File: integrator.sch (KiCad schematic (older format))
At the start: 13 parts, among them J1 SJ-3524-SMT, J2 SJ-3524-SMT, SW1 EVQP40B3M, SW2 EVQP40B3M, U1 Teensy3.2, U2 FXOS8700CQ

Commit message: saved before library tweak
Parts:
- removed C1, C2, C3: 0.1uF, Capacitor_SMD:C_0603_1608Metric, symbol Device:CP1_Small
- removed U2: FXOS8700CQ, misc:FSOS8700CQ_PKG, symbol FXOS8700CQ:FXOS8700CQ
- added C1: 10nf, symbol Device:C_Small
- added C2, C5: 0.1uf, symbol Device:C_Small
- added C3: 2.2uf, symbol Device:C_Small
- added C4: 4.7uf, symbol Device:C_Small
- added D1: SD0805S020S1R0, symbol Device:D_Schottky_Small
- added R2, R3, R6: 4.7k, symbol Device:R
- added R4, R5: 5k, symbol Device:R
- added U2: ICM-20600, PQFN50P250X300X97-14N, symbol icm-20600:ICM-20600
- POGO1: value Conn_02x06_Odd_Even_MountingPin -> PO pogos
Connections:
- wire segments 108 -> 136
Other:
- moved on the sheet: J2, LED1, LED2, R1, SW1

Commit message: snapshot everything for safety
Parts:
- added C6: 4.7uf, Capacitor_SMD:CP_Elec_5x4.5, symbol Device:C_Small
- C1, C2, C3, C5: footprint (none) -> Capacitor_SMD:C_0805_2012Metric
- C4: footprint (none) -> Capacitor_SMD:CP_Elec_5x4.5
- D1: footprint (none) -> Diode_SMD:D_0805_2012Metric
- LED1, LED2: footprint LED_SMD:LED_0603_1608Metric -> LED_SMD:LED_0805_2012Metric
- POGO1: footprint Connector_PinSocket_2.54mm:PinSocket_2x06_P2.54mm_Vertical -> Connector_PinSocket_2.54mm:PinSocket_2x06_P2.54mm_Vertical_SMD
- R1: footprint Resistor_SMD:R_0603_1608Metric -> Resistor_SMD:R_0805_2012Metric
- R2, R3, R4, R5, R6: footprint (none) -> Resistor_SMD:R_0805_2012Metric
- U2: symbol icm-20600:ICM-20600 -> ICM-20600:ICM-20600
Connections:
- net Earth: now also SW2.2, C6.2; no longer SW2.1
- net at U1.11 (9_RX2_CS_PWM): now also SW2.1; no longer SW2.2
- net at C1.2, C2.1, C3.1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: now also C4.1, D1.1 (K), U1.31 (3.3V), C6.1; no longer U1.16 (3.3V)
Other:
- moved on the sheet: C1, C2, C3, C4, C5, D1, J1, J2, LED1, LED2, POGO1, R1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

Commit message: snapshot with hackzone
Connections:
- net at U1.2 (0_RX1_Touch): now also SW1.2
- net at U1.5 (3_TX_PWM): no longer SW1.2
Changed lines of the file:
@@
 	6000 2250 1800 2250
-Wire Wire Line
-	6500 3800 6000 3800
-Wire Wire Line
-	6000 3800 6000 2250
 Wire Wire Line
 	2750 1250 5600 1250
@@
 Wire Wire Line
 	8800 6100 8900 6150
-Wire Wire Line
-	6500 3600 5050 3600
-Wire Wire Line
-	5050 3600 5050 3500
-Wire Wire Line
-	5050 3500 1700 3500
 Wire Wire Line
 	1700 3500 1700 4700
@@
 	8600 5900 8800 5900
 Connection ~ 5400 4900
+Wire Wire Line
+	5050 3500 1700 3500
+Wire Wire Line
+	5050 3600 5050 3500
+Wire Wire Line
+	6500 3600 5050 3600
+Wire Wire Line
+	6500 3500 6000 3500
+Wire Wire Line
+	6000 3500 6000 2250
 $EndSCHEMATC

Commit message: last changes of rev3
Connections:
- net r_sync_out: now reaches J2.2, U1.10 (8_TX3_DIN)
- net r_button: now reaches SW2.1, U1.11 (9_RX2_CS_PWM)
- net l_sync_out: now reaches J1.2, U1.13 (11_DOUT)
- net dac: now reaches R4.1, R5.2, U1.19 (A14/DAC)
- net l_button: now reaches SW1.2, U1.2 (0_RX1_Touch)
- net po_play: now reaches POGO1.12 (Pin_12), U1.23 (16_A2_SCL0_Touch)
- net po_wake: now reaches POGO1.6 (Pin_6), U1.24 (17_A3_SDA0_Touch)
- net i2c_sda: now reaches R3.2, U1.25 (18_A4_SDA0_Touch), U2.14 (SDA/SDI)
- net i2c_clk: now reaches R2.2, U1.26 (19_A5_SCL0_Touch), U2.13 (SCL/SCLK)
- net led1: now reaches LED1.2, U1.27 (20_A6_CS_PWM)
- net led2: now reaches LED2.2, U1.28 (21_A7_RX1_CS_PWM)
- net amu_sync: now reaches U1.3 (1_TX1_Touch), U2.10 (FSYNC/NC)
- net +3.3v: now reaches C1.2, C2.1, C3.1, C4.1, C6.1, D1.1 (K), R2.1, R3.1, U1.31 (3.3V), U2.12 (~CS), U2.5 (VDDIO), U2.8 (VDD)
- net a_gnd: now reaches J1.1, J2.1, U1.32 (AGND)
- net amu_int2: now reaches U1.4 (2), U2.9 (INT2)
- net swo: now reaches POGO1.9 (Pin_9), U1.6 (4_RX_PWM)
- net swdio: now reaches POGO1.7 (Pin_7), U1.7 (5_TX1_PWM)
- net swclk: now reaches POGO1.5 (Pin_5), U1.8 (6_PWM)
- net po_reset: now reaches POGO1.3 (Pin_3), R6.2, U1.9 (7_RX3_DOUT)
- net po_batt: now reaches D1.2 (A), POGO1.4 (Pin_4)
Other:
- moved on the sheet: C1, C2, C3, C4, C5, C6, D1, J1, J2, LED1, LED2, POGO1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

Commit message: evt4 schem w/o rocker switches
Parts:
- removed C5: 0.1uf, Capacitor_SMD:C_0805_2012Metric, symbol Device:C_Small
- removed R3: 4.7k, Resistor_SMD:R_0805_2012Metric, symbol Device:R
- added SW3: SW_Push_LED, symbol Switch:SW_Push_LED
- R2: value 4.7k -> 47
- U2: value ICM-20600 -> ICM-42605; footprint PQFN50P250X300X97-14N -> PQFN50P300X250X97-14N; symbol ICM-20600:ICM-20600 -> ICM-42605:ICM-42605; MANUFACTURER (none) -> TDK Corporation; MP ICM-20600 -> ICM-42605; PARTREV (none) -> 0.4; STANDARD (none) -> IPC 7351B
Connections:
- net +3.3v: no longer C1.2, C2.1, C3.1, C4.1, C6.1, D1.1 (K), R2.1, U1.31 (3.3V), U2.12 (~CS), U2.5 (VDDIO), U2.8 (VDD)
- net Earth: now also R2.1, U2.10 (RESV_4), U2.11 (RESV_5), U2.2 (RESV_1), U2.3 (RESV_2), U2.9 (INT2/FSYNC), SW3.1; no longer U2.1 (AD0/SDO)
- net a_gnd: no longer J1.1, J2.1, U1.32 (AGND)
- net amu_int2: no longer U1.4 (2), U2.9 (INT2)
- net l_button: no longer SW1.2, U1.2 (0_RX1_Touch)
- net l_sync_out: now also U1.27 (20_A6_CS_PWM); no longer U1.13 (11_DOUT)
- net led1: no longer LED1.2, U1.27 (20_A6_CS_PWM)
- net led2: no longer LED2.2, U1.28 (21_A7_RX1_CS_PWM)
- net po_reset: now also R6.1; no longer R6.2
- net po_wake: now also U1.11 (9_RX2_CS_PWM); no longer U1.24 (17_A3_SDA0_Touch)
- net r_button: no longer SW2.1, U1.11 (9_RX2_CS_PWM)
- net r_sync_out: no longer J2.2, U1.10 (8_TX3_DIN)
- net at U1.12 (10_TX2_CS_PWM): now also U2.12 (AP_CS)
- net at U1.14 (12_DIN): now also U2.1 (AP_SDO/AP_ADO)
- net at U1.20 (13_LED_SCK): now also U2.13 (AP_SCL/AP_SCLK)
- net at U1.22 (15_A1_CS_Touch): now also LED1.2
- net at U1.29 (22_A8_Touch_PWM): now also SW2.1
- net at U1.30 (23_A9_Touch_PWM): now also J2.2
- net at POGO1.1 (Pin_1): now also R6.2
- net at POGO1.11 (Pin_11): no longer R6.1
- net at U2.4 (INT1/INT): now also U1.4 (2)
- net amu_sync renamed NONSTOP_LED
- net NONSTOP_LED: now also SW3.4 (A); no longer U2.10 (FSYNC/NC)
- removed net i2c_clk: R2.2, U1.26 (19_A5_SCL0_Touch), U2.13 (SCL/SCLK)
- net i2c_sda: no longer names the net of U2.14 (AP_SDA/AP_SDIO/AP_SDI)
- net i2c_sda: now also U1.13 (11_DOUT); no longer U1.25 (18_A4_SDA0_Touch)
- new net: LED2.2, U1.10 (8_TX3_DIN)
- new net: SW3.2, U1.2 (0_RX1_Touch)
- new net: SW1.2, U1.28 (21_A7_RX1_CS_PWM)
- new net: C1.2, C2.1, C3.1, C4.1, C6.1, D1.1 (K), U1.31 (3.3V), U2.5 (VDDIO), U2.8 (VDD)
- new net: J1.1, J2.1, U1.32 (AGND)
- new net: R2.2, SW3.3 (K)
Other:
- moved on the sheet: C1, C2, C3, C4, C6, D1, POGO1, R6

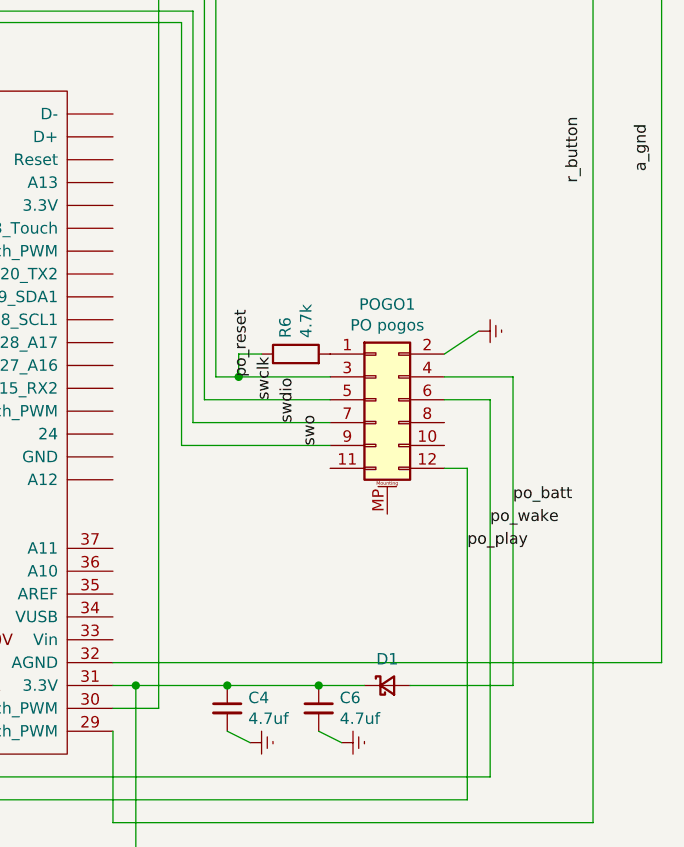
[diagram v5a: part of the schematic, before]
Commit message: 5x2 pogo
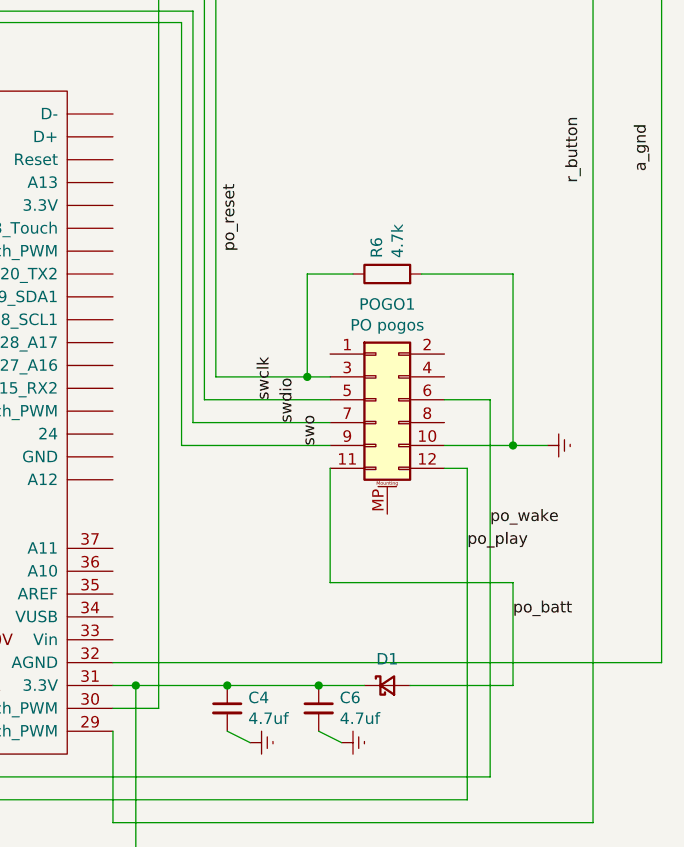
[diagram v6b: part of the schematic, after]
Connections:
- net Earth: now also POGO1.10 (Pin_10), R6.2; no longer POGO1.2 (Pin_2)
- net po_batt: now also POGO1.11 (Pin_11); no longer POGO1.4 (Pin_4)
- net po_reset: no longer POGO1.3 (Pin_3), R6.1, U1.9 (7_RX3_DOUT)
- net at POGO1.1 (Pin_1): no longer R6.2
- new net: POGO1.3 (Pin_3), R6.1, U1.9 (7_RX3_DOUT)
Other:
- moved on the sheet: R6
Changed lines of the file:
@@
 L power:Earth #PWR0102
 U 1 1 6012BDBE
-P 9650 4400
-F 0 "#PWR0102" H 9650 4150 50  0001 C CNN
-F 1 "Earth" H 9650 4250 50  0001 C CNN
-F 2 "" H 9650 4400 50  0001 C CNN
-F 3 "~" H 9650 4400 50  0001 C CNN
-	1    9650 4400
+P 9950 4900
+F 0 "#PWR0102" H 9950 4650 50  0001 C CNN
+F 1 "Earth" H 9950 4750 50  0001 C CNN
+F 2 "" H 9950 4900 50  0001 C CNN
+F 3 "~" H 9950 4900 50  0001 C CNN
+	1    9950 4900
 	0    -1   -1   0
 $EndComp
 Wire Wire Line
-	9500 4500 9650 4400
-Wire Wire Line
-	9800 4600 9500 4600
+	9800 4900 9950 4900
 Wire Wire Line
 	9500 4700 9700 4700
@@
 Wire Wire Line
 	8550 1900 8550 1600
-Wire Wire Line
-	9800 4600 9800 5950
 $Comp
 L Device:R R6
 U 1 1 6054846D
-P 8850 4500
-F 0 "R6" H 8920 4546 50  0000 L CNN
-F 1 "4.7k" H 8920 4455 50  0000 L CNN
-F 2 "Resistor_SMD:R_0805_2012Metric" V 8780 4500 50  0001 C CNN
-F 3 "~" H 8850 4500 50  0001 C CNN
-	1    8850 4500
+P 9250 4150
+F 0 "R6" H 9320 4196 50  0000 L CNN
+F 1 "4.7k" H 9320 4105 50  0000 L CNN
+F 2 "Resistor_SMD:R_0805_2012Metric" V 9180 4150 50  0001 C CNN
+F 3 "~" H 9250 4150 50  0001 C CNN
+	1    9250 4150
 	0    -1   -1   0
 $EndComp
-Wire Wire Line
-	8500 4600 8600 4600
-Connection ~ 8600 4600
 $Comp
 L Device:C_Small C1
@@
 Text Label 5900 6800 0    50   ~ 0
 +3.3v
-Text Label 9800 5150 0    50   ~ 0
-po_batt
 Text Label 9700 5250 0    50   ~ 0
 po_wake
 Text Label 9600 5350 0    50   ~ 0
 po_play
-Text Label 8650 4600 1    50   ~ 0
+Text Label 8600 4050 1    50   ~ 0
 po_reset
-Wire Wire Line
-	8600 4600 9000 4600
 Text Label 2850 6300 1    50   ~ 0
 led1
@@
 Wire Wire Line
 	2750 5900 2750 6400
-Wire Wire Line
-	8700 4500 8600 4500
-Wire Wire Line
-	8600 4500 8600 4600
 Text Label 8750 4700 1    50   ~ 0
 swclk
@@
 Text Label 5900 2300 3    50   ~ 0
 NONSTOP_LED
+Wire Wire Line
+	9000 5000 9000 5500
+Wire Wire Line
+	9000 5500 9800 5500
+Wire Wire Line
+	9800 5500 9800 5950
+Text Label 9800 5650 0    50   ~ 0
+po_batt
+Wire Wire Line
+	9400 4150 9800 4150
+Wire Wire Line
+	9800 4150 9800 4900
+Wire Wire Line
+	9800 4900 9500 4900
+Wire Wire Line
+	8900 4600 8900 4150
+Wire Wire Line
+	8900 4150 9100 4150
+Connection ~ 8900 4600
+Wire Wire Line
+	8900 4600 9000 4600
+Wire Wire Line
+	8500 4600 8900 4600
+Connection ~ 9800 4900
 $EndSCHEMATC

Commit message: evt4 pcb layout
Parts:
- SW3: footprint (none) -> TL3215AF160BQ:E-Switch-N326000-0-0-0; symbol Switch:SW_Push_LED -> TL3215AF160BQ:TL3215AF160BQ
- U2: footprint PQFN50P300X250X97-14N -> ICM-42605:PQFN50P300X250X97-14N
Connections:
- net +3.3v: now also C1.2, C2.1, C3.1, C4.1, C6.1, D1.1 (K), U1.31 (3.3V), U2.5 (VDDIO), U2.8 (VDD)
- net Earth: now also SW3.4; no longer SW3.1
- net a_gnd: now also J1.1, J2.1, U1.32 (AGND)
- net led1: now also LED1.2, U1.22 (15_A1_CS_Touch)
- net led2: now also LED2.2, U1.10 (8_TX3_DIN)
- net po_reset: now also POGO1.3 (Pin_3), R6.1, U1.9 (7_RX3_DOUT)
- net r_sync_out: now also J2.2, U1.30 (23_A9_Touch_PWM)
- net spi_cs: now reaches U1.12 (10_TX2_CS_PWM), U2.12 (AP_CS)
- net spi_mosi: now reaches U1.13 (11_DOUT), U2.14 (AP_SDA/AP_SDIO/AP_SDI)
- net spi_miso: now reaches U1.14 (12_DIN), U2.1 (AP_SDO/AP_ADO)
- net nonstop_sw: now reaches SW3.2, U1.2 (0_RX1_Touch)
- net spi_clock: now reaches U1.20 (13_LED_SCK), U2.13 (AP_SCL/AP_SCLK)
- net sw1: now reaches SW1.2, U1.28 (21_A7_RX1_CS_PWM)
- net sw2: now reaches SW2.1, U1.29 (22_A8_Touch_PWM)
- net imu_int1: now reaches U1.4 (2), U2.4 (INT1/INT)
- net at SW3.3: no longer R2.2
- net NONSTOP_LED renamed nonstop_led
- net nonstop_led: now also SW3.6 (+); no longer SW3.4 (A)
- new net: R2.2, SW3.5 (-)
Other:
- moved on the sheet: D1, LED1, LED2, R1
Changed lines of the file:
@@
 L 2021-01-16_04-43-04:LS_L29K-G1J2-1-Z LED2
 U 1 1 6002719A
-P 2150 7100
-F 0 "LED2" H 2350 6925 60  0000 C CNN
-F 1 "LS_L29K-G1J2-1-Z" H 2350 6800 60  0000 C CNN
-F 2 "LED_SMD:LED_0805_2012Metric" H 2350 6740 60  0001 C CNN
-F 3 "" H 2150 7100 60  0000 C CNN
-	1    2150 7100
+P 2150 7600
+F 0 "LED2" H 2350 7425 60  0000 C CNN
+F 1 "LS_L29K-G1J2-1-Z" H 2350 7300 60  0000 C CNN
+F 2 "LED_SMD:LED_0805_2012Metric" H 2350 7240 60  0001 C CNN
+F 3 "" H 2150 7600 60  0000 C CNN
+	1    2150 7600
 	-1   0    0    1
 $EndComp
@@
 L 2021-01-16_04-43-04:LS_L29K-G1J2-1-Z LED1
 U 1 1 60027292
-P 2150 6400
-F 0 "LED1" H 2350 6225 60  0000 C CNN
-F 1 "LS_L29K-G1J2-1-Z" H 2350 6100 60  0000 C CNN
-F 2 "LED_SMD:LED_0805_2012Metric" H 2350 6040 60  0001 C CNN
-F 3 "" H 2150 6400 60  0000 C CNN
-	1    2150 6400
+P 2150 6900
+F 0 "LED1" H 2350 6725 60  0000 C CNN
+F 1 "LS_L29K-G1J2-1-Z" H 2350 6600 60  0000 C CNN
+F 2 "LED_SMD:LED_0805_2012Metric" H 2350 6540 60  0001 C CNN
+F 3 "" H 2150 6900 60  0000 C CNN
+	1    2150 6900
 	-1   0    0    1
 $EndComp
@@
 L Device:R R1
 U 1 1 60027645
-P 1200 6800
-F 0 "R1" V 1280 6800 50  0000 C CNN
-F 1 "47" V 1200 6800 50  0000 C CNN
-F 2 "Resistor_SMD:R_0805_2012Metric" V 1130 6800 50  0001 C CNN
-F 3 "" H 1200 6800 50  0000 C CNN
-	1    1200 6800
+P 1200 7300
+F 0 "R1" V 1280 7300 50  0000 C CNN
+F 1 "47" V 1200 7300 50  0000 C CNN
+F 2 "Resistor_SMD:R_0805_2012Metric" V 1130 7300 50  0001 C CNN
+F 3 "" H 1200 7300 50  0000 C CNN
+	1    1200 7300
 	0    1    1    0
 $EndComp
@@
 L power:Earth #PWR013
 U 1 1 6002774C
-P 900 6900
-F 0 "#PWR013" H 900 6650 50  0001 C CNN
-F 1 "Earth" H 900 6750 50  0001 C CNN
-F 2 "" H 900 6900 50  0000 C CNN
-F 3 "" H 900 6900 50  0000 C CNN
-	1    900  6900
-	0    1    1    0
-$EndComp
-Wire Wire Line
-	1750 6400 1400 6400
-Wire Wire Line
-	1400 6400 1400 6800
-Wire Wire Line
-	1400 6800 1350 6800
-Wire Wire Line
-	1400 7100 1750 7100
-Connection ~ 1400 6800
-Wire Wire Line
-	1050 6800 900  6900
+P 900 7400
+F 0 "#PWR013" H 900 7150 50  0001 C CNN
+F 1 "Earth" H 900 7250 50  0001 C CNN
+F 2 "" H 900 7400 50  0000 C CNN
+F 3 "" H 900 7400 50  0000 C CNN
+	1    900  7400
+	0    1    1    0
+$EndComp
+Wire Wire Line
+	1750 6900 1400 6900
+Wire Wire Line
+	1400 6900 1400 7300
+Wire Wire Line
+	1400 7300 1350 7300
+Wire Wire Line
+	1400 7600 1750 7600
+Connection ~ 1400 7300
+Wire Wire Line
+	1050 7300 900  7400
 Wire Wire Line
 	8650 2500 8550 2400
@@
 	1250 2700 1250 2800
 Wire Wire Line
-	1400 6800 1400 7100
+	1400 7300 1400 7600
 $Comp
 L power:Earth #PWR0101
@@
 Wire Wire Line
 	1100 4250 1000 4200
-Wire Wire Line
-	9350 5950 9800 5950
-$Comp
-L Device:D_Schottky_Small D1
-U 1 1 606BFC3B
-P 9250 5950
-F 0 "D1" H 9250 6065 50  0000 C CNN
-F 1 "SD0805S020S1R0" H 9250 6066 50  0001 C CNN
-F 2 "Diode_SMD:D_0805_2012Metric" V 9250 5950 50  0001 C CNN
-F 3 "~" V 9250 5950 50  0001 C CNN
-	1    9250 5950
-	1    0    0    -1
-$EndComp
 $Comp
 L Device:C_Small C4
@@
 Connection ~ 8950 5950
 Wire Wire Line
-	8950 5950 9150 5950
-Wire Wire Line
-	2750 7100 2150 7100
-Wire Wire Line
-	2750 7100 2750 6550
-Wire Wire Line
-	2150 6400 2750 6400
+	8950 5950 8950 5750
 $Comp
 L power:Earth #PWR06
@@
 Wire Wire Line
 	8150 5950 8150 6700
-Text Label 5900 6800 0    50   ~ 0
-+3.3v
-Text Label 9700 5250 0    50   ~ 0
+Text Label 9700 5400 1    50   ~ 0
 po_wake
-Text Label 9600 5350 0    50   ~ 0
-po_play
-Text Label 8600 4050 1    50   ~ 0
-po_reset
-Text Label 2850 6300 1    50   ~ 0
-led1
-Text Label 2850 6650 3    50   ~ 0
-led2
-Text Label 8200 2200 1    50   ~ 0
-r_sync_out
 Text Label 4850 1700 3    50   ~ 0
 l_sync_out
-Text Label 10100 3750 1    50   ~ 0
-r_button
-Text Label 5400 3450 1    50   ~ 0
-l_button
 Text Label 4850 1500 1    50   ~ 0
 dac
 Wire Wire Line
-	5800 6550 2750 6550
-Wire Wire Line
 	5100 1700 2250 1700
 Wire Wire Line
@@
 Wire Wire Line
 	4600 3750 6050 3750
-Text Label 4550 4550 1    50   ~ 0
-amu_int2
 $Comp
 L ICM-42605:ICM-42605 U2
@@
 F 0 "U2" H 2100 5517 50  0000 C CNN
 F 1 "ICM-42605" H 2100 5426 50  0000 C CNN
-F 2 "PQFN50P300X250X97-14N" H 2100 4650 50  0001 L BNN
+F 2 "ICM-42605:PQFN50P300X250X97-14N" H 2100 4650 50  0001 L BNN
 F 3 "" H 2100 4650 50  0001 L BNN
 F 4 "ICM-42605" H 2100 4650 50  0001 L BNN "MP"
@@
 	950  4650 1100 4650
 Wire Wire Line
-	1100 4550 850  4550
-Wire Wire Line
-	850  4550 850  5450
-Wire Wire Line
-	850  5450 4950 5450
-Wire Wire Line
-	4950 5450 4950 4550
-Wire Wire Line
-	4950 4550 6050 4550
-Wire Wire Line
-	5050 4750 5050 5550
-Wire Wire Line
-	5050 5550 1050 5550
-Wire Wire Line
-	1050 5550 1050 4850
+	1100 4550 900  4550
+Wire Wire Line
+	900  4550 900  5400
+Wire Wire Line
+	900  5400 4750 5400
+Wire Wire Line
+	4750 5400 4750 4550
+Wire Wire Line
+	4750 4550 6050 4550
+Wire Wire Line
+	4700 4750 4700 5450
+Wire Wire Line
+	4700 5450 1050 5450
+Wire Wire Line
+	1050 5450 1050 4850
 Wire Wire Line
 	1050 4850 1100 4850
 Wire Wire Line
-	6050 4750 5050 4750
-Wire Wire Line
-	6050 4650 5250 4650
-Wire Wire Line
-	5250 4650 5250 5650
-Wire Wire Line
-	5250 5650 1000 5650
-Wire Wire Line
-	1000 5650 1000 4750
+	6050 4750 4700 4750
+Wire Wire Line
+	6050 4650 4850 4650
+Wire Wire Line
+	4850 4650 4850 5500
+Wire Wire Line
+	4850 5500 1000 5500
+Wire Wire Line
+	1000 5500 1000 4750
 Wire Wire Line
 	1000 4750 1100 4750
@@
 Connection ~ 8150 5950
 Wire Wire Line
-	8050 5850 10450 5850
-Wire Wire Line
 	10450 1900 10450 5850
 Wire Wire Line
@@
 Wire Wire Line
 	5100 1700 5100 6050
-Text Label 10400 3700 1    50   ~ 0
-a_gnd
-Wire Wire Line
-	5800 6550 5800 4350
+Wire Wire Line
+	5800 7600 5800 4350
 Wire Wire Line
 	5800 4350 6050 4350
@@
 	5100 6050 6050 6050
 Wire Wire Line
-	2750 5900 5700 5900
-Wire Wire Line
-	5700 5900 5700 5550
-Wire Wire Line
-	5700 5550 6050 5550
-Wire Wire Line
-	2750 5900 2750 6400
+	5750 6900 5750 5550
+Wire Wire Line
+	5750 5550 6050 5550
 Text Label 8750 4700 1    50   ~ 0
 swclk
@@
 swo
 $Comp
-L Switch:SW_Push_LED SW3
+L TL3215AF160BQ:TL3215AF160BQ SW3
 U 1 1 6111973C
-P 6700 2050
-F 0 "SW3" H 6700 1810 50  0000 C CNN
-F 1 "SW_Push_LED" H 6700 1901 50  0000 C CNN
-F 2 "" H 6700 2350 50  0001 C CNN
-F 3 "~" H 6700 2350 50  0001 C CNN
-	1    6700 2050
-	-1   0    0    1
+P 6100 2550
+F 0 "SW3" H 6600 2700 50  0000 C CNN
+F 1 "SW_Push_LED" H 6600 1800 50  0000 C CNN
+F 2 "TL3215AF160BQ:E-Switch-N326000-0-0-0" H 6100 2850 50  0001 C CNN
+F 3 "~" H 6100 2850 50  0001 C CNN
+	1    6100 2550
+	1    0    0    1
 $EndComp
 Wire Wire Line
@@
 	6050 3550 5950 3550
 Wire Wire Line
-	5950 3550 5950 2150
-Wire Wire Line
-	5950 2150 6500 2150
+	5950 3550 5950 2350
+Wire Wire Line
+	5950 2350 6200 2350
 Wire Wire Line
 	6050 3650 5900 3650
@@
 	5900 3650 5900 2050
 Wire Wire Line
-	5900 2050 6500 2050
+	5900 2050 6200 2050
 $Comp
 L Device:R R2
@@
 $EndComp
 Wire Wire Line
-	6900 2050 7050 2050
+	7000 2050 7050 2050
 Wire Wire Line
 	7350 2050 7500 2050
 Wire Wire Line
-	6900 2150 7500 2150
-Wire Wire Line
-	7500 2150 7500 2050
+	7000 2350 7500 2350
+Wire Wire Line
+	7500 2350 7500 2050
 Connection ~ 7500 2050
-Text Label 6050 2800 1    50   ~ 0
-NONSTOP_SW
-Text Label 5900 2300 3    50   ~ 0
-NONSTOP_LED
-Wire Wire Line
-	9000 5000 9000 5500
-Wire Wire Line
-	9000 5500 9800 5500
-Wire Wire Line
-	9800 5500 9800 5950
-Text Label 9800 5650 0    50   ~ 0
+Text Label 8950 5300 3    50   ~ 0
 po_batt
 Wire Wire Line
@@
 	8500 4600 8900 4600
 Connection ~ 9800 4900
+Wire Wire Line
+	8050 5850 10450 5850
+$Comp
+L Device:D_Schottky_Small D1
+U 1 1 606BFC3B
+P 8950 5650
+F 0 "D1" H 8950 5765 50  0000 C CNN
+F 1 "SD0805S020S1R0" H 8950 5766 50  0001 C CNN
+F 2 "Diode_SMD:D_0805_2012Metric" V 8950 5650 50  0001 C CNN
+F 3 "~" V 8950 5650 50  0001 C CNN
+	1    8950 5650
+	0    -1   -1   0
+$EndComp
+Wire Wire Line
+	8950 5000 9000 5000
+Wire Wire Line
+	8950 5000 8950 5550
+Wire Wire Line
+	2150 7600 5800 7600
+Wire Wire Line
+	2150 6900 5750 6900
+Text Label 900  4900 3    50   ~ 0
+spi_cs
+Text Label 1450 5350 2    50   ~ 0
+spi_clock
+Text Label 1000 5500 3    50   ~ 0
+spi_mosi
+Text Label 4700 4900 3    50   ~ 0
+spi_miso
+Text Label 4600 4100 3    50   ~ 0
+imu_int1
+Text Label 5450 5700 3    50   ~ 0
+sw1
+Text Label 10000 6550 2    50   ~ 0
+sw2
+Text Label 10450 3550 3    50   ~ 0
+a_gnd
+Text Label 8250 1950 3    50   ~ 0
+r_sync_out
+Text Label 6000 2350 3    50   ~ 0
+nonstop_sw
+Text Label 5900 2400 3    50   ~ 0
+nonstop_led
+Text Label 8500 3800 0    50   ~ 0
+po_reset
+Text Label 9600 5350 3    50   ~ 0
+po_play
+Text Label 6500 6700 2    50   ~ 0
++3.3v
+Text Label 2950 6900 2    50   ~ 0
+led1
+Text Label 2950 7600 2    50   ~ 0
+led2
 $EndSCHEMATC
